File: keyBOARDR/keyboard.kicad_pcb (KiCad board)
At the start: 2 copper layers, 141.2 x 114.2 mm, 52 parts, among them J4 AudioJack4, J5 JT8P-3.2T- -1-16Y, SW1 SW_MEC_5G, SW10 SW_MEC_5G, SW11 SW_MEC_5G, SW12 SW_MEC_5G, SW13 SW_MEC_5G, SW14 SW_MEC_5G, SW15 SW_MEC_5G, SW16 SW_key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

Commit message: Right part of NEW version and
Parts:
- D10, D13: moved to F.Cu
- moved SW15 0.93 mm to (165.0, 97.5)
- moved SW9 0.93 mm to (165.0, 78.5)
- moved SW11 0.93 mm to (126.9, 78.5)
- moved SW17 0.93 mm to (126.9, 97.5)
- moved SW22 0.93 mm to (88.5, 136.3)
- moved SW10 0.93 mm to (145.9, 78.5)
- moved SW12 0.93 mm to (107.8, 78.5)
- moved SW13 0.93 mm to (203.1, 97.5)
- moved SW14 0.93 mm to (184.0, 97.5)
- moved SW16 0.93 mm to (145.9, 97.5)
- moved SW18 0.93 mm to (107.8, 97.5)
- moved SW7 0.93 mm to (203.1, 78.5)
- moved SW8 0.93 mm to (184.0, 78.5)
- moved SW3 0.93 mm to (165.0, 59.4)
- moved SW5 0.93 mm to (126.9, 59.4)
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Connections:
- J4 pad R1: GPIO0 -> GPIO1
- J4 pad R2: GPIO1 -> GPIO0
- J4 pad T: VSYS -> +3.3V
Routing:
- net col1: track 0.00 -> 224.5 mm, vias 0 -> 1
- net col2: track 0.00 -> 202.9 mm, vias 0 -> 1
- net row1: track 0.00 -> 177.6 mm
- net row2: track 0.00 -> 156.9 mm
- net row3: track 0.00 -> 148.2 mm
- net rowX: track 0.00 -> 133.9 mm
- net colX1: track 0.00 -> 115.8 mm
- net +3.3V: track 0.00 -> 106.5 mm
- net colX2: track 0.00 -> 95.0 mm
- net colX4: track 0.00 -> 80.3 mm
- net colX3: track 0.00 -> 74.8 mm
- net col6: track 0.00 -> 50.4 mm
- net col3: track 0.00 -> 40.3 mm
- net col5: track 0.00 -> 40.0 mm
- net col4: track 0.00 -> 39.9 mm
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
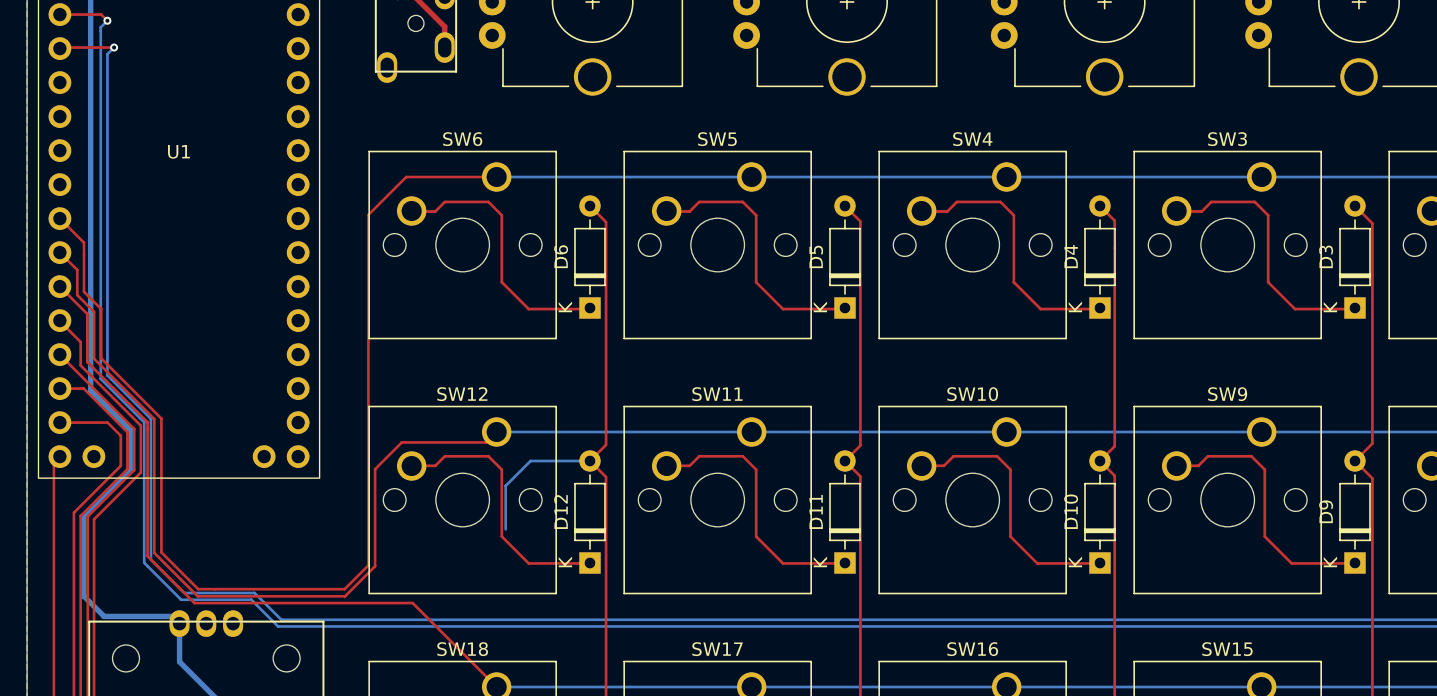
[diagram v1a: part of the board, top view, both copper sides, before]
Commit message: connect Keys and board
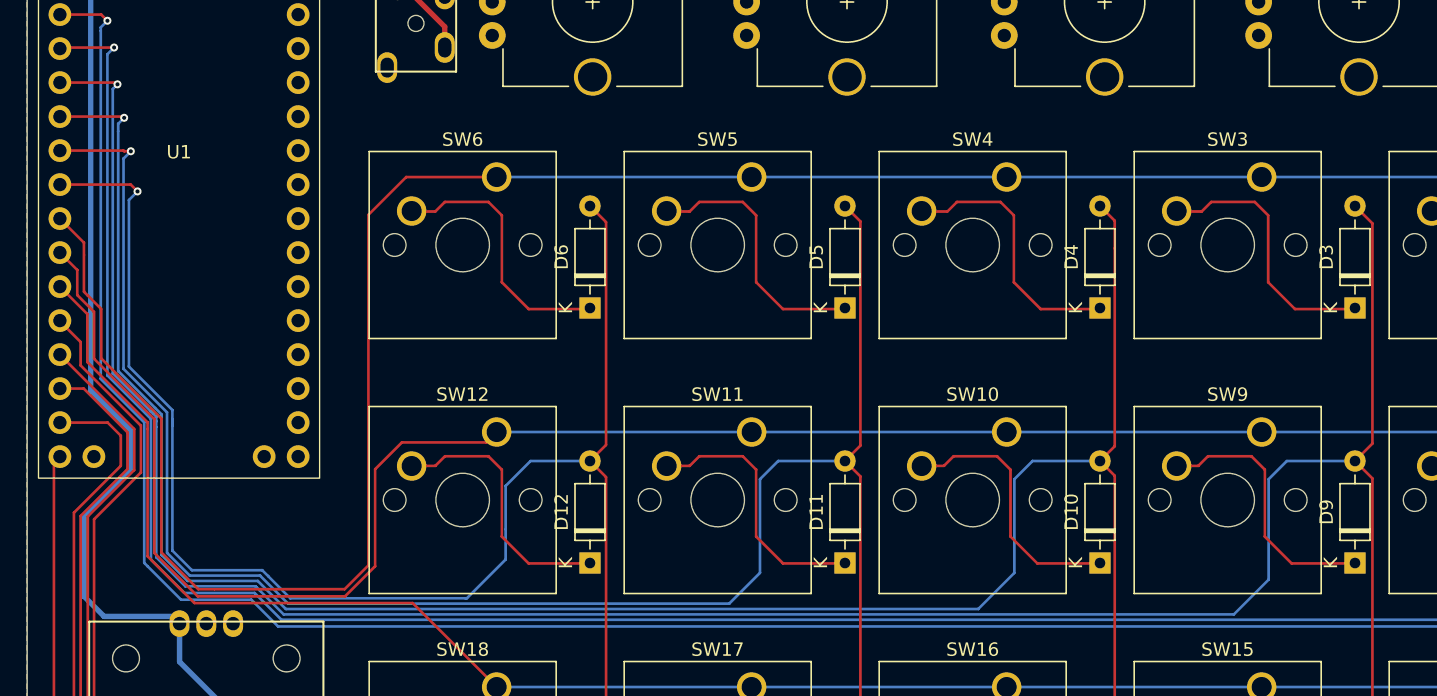
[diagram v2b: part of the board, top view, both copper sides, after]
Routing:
- net col3: track 40.3 -> 181.9 mm, vias 0 -> 1
- net col4: track 39.9 -> 159.4 mm, vias 0 -> 1
- net col5: track 40.0 -> 137.6 mm, vias 0 -> 1
- net col6: track 50.4 -> 115.2 mm, vias 0 -> 1

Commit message: swap lotery encoders and connect some
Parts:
- moved SW23 71.7 mm to (198.0, 48.9), turned to 180 degrees
- moved SW26 43.0 mm to (140.8, 48.9), turned to 180 degrees
- moved SW24 33.6 mm to (179.0, 48.9), turned to 180 degrees
- moved SW27 15.3 mm to (122.0, 48.9), turned to 180 degrees
- moved SW25 7.07 mm to (159.8, 48.9), turned to 180 degrees
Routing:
- net GPIO24: track 0.00 -> 36.0 mm
- net GPIO25: track 0.00 -> 33.6 mm

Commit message: i
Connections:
- J4 pad T: +3.3V -> VSYS
- U1 pad 18: unconnected-(U1-GND-Pad18) -> GND
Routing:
- net GPIO16: track 0.00 -> 123.8 mm
- net GPIO17: track 0.00 -> 123.8 mm
- net GPIO18: track 0.00 -> 100.9 mm
- net GPIO19: track 0.00 -> 100.8 mm
- net GPIO20: track 0.00 -> 77.2 mm
- net GPIO21: track 0.00 -> 77.2 mm
- net GPIO26: track 0.00 -> 61.5 mm, vias 0 -> 1
- net GPIO23: track 0.00 -> 54.4 mm
- net GPIO22: track 0.00 -> 54.0 mm
- net GPIO27: track 0.00 -> 47.2 mm, vias 0 -> 1
- net VSYS: track 0.00 -> 38.3 mm
- net +3.3V: track 106.5 -> 90.5 mm
- net GPIO24: track 36.0 -> 32.6 mm
- net col6: track 115.2 -> 112.2 mm
- net col5: track 137.6 -> 134.7 mm
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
